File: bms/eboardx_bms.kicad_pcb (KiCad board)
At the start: 2 copper layers, 56 x 60 mm, 171 parts, among them J1 Balance connector, P1 CONN_1, P2 CONN_1, P3 CONN_1, P4 CONN_1, Q1 MMBT3904, Q10 SE4060GB, Q11 SE4060GB, Q12 SE4060GB, Q13 SE4060GB, Q14 MMBT3904, Q15 MMBT3906, Q16 MMBT3906, Q17 MMBT3906, Q18 MMBT3906, Q19 MMBT3906, Q2 SE4060GB, Q20 MMBT3906, Q21 MMBT3906, Q22 MMBT3906, Q23 MMBT3906, Q24 MMBT3906, Q25 MMBT3906, Q26 MMBT3906, Q27 A2SHB, Q28 A2SHB, Q29 A2SHB, Q3 SE4060GB, Q30 A2SHB, Q31 A2SHB, Q32 A2SHB, Q33 MMBT3906, Q34 MMBT3906, Q35 MMBT3906, Q36 MMBT3906, Q37 MMBT3906, Q38 MMBT3906, Q39 MMBT3906, Q4 SE4060GB, Q40 MMBT3906, Q41 A2SHB, Q42 A2SHB, Q43 A2SHB, Q44 A2SHB, Q5 SE4060GB, Q6 SE4060GB, Q7 SE4060GB, Q8 SE4060GB, Q9 SE4060GB, U1 DW01A, U10 HY2213-xxxA, U11 HY2213-xxxA, U12 HY2213-xxxA, U13 DW01A, U14 DW01A, U15 DW01A, U16 DW01A, U17 HY2213-xxxA, U18 HY2213-xxxA, U19 HY2213-xxxA, U2 DW01A, U20 HY2213-xxxA, U3 DW01A, U4 DW01A, U5 DW01A, U6 DW01A, U7 HY2213-xxxA, U8 HY2213-xxxA, U9 HY2213-xxxA

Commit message: bms
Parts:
- C14, C15, C16, C17, C2, C3, C4, C5, C6, C7, Q15, Q16, Q17, Q18, Q19, Q20, Q21, Q22, Q23, Q24, Q25, Q26, Q33, Q34, Q35, Q36, Q37, Q38, Q39, Q40, R10, R11, R12, R13, R14, R15, R16, R17, R18, R19, R20, R21, R22, R23, R24, R25, R26, R27, R28, R29, R30, R31, R32, R33, R34, R35, R36, R37, R38, R51, R52, R53, R54, R55, R56, R57, R58, R59, R60, R61, R62, R63, R64, R65, R66, R67, R69, R70, R71, R72, R9, U1, U13, U14, U15, U16, U2, U3, U4, U5, U6: moved to B.Cu
- P1: value CONN_1 -> BAT+
- P2: value CONN_1 -> P+
- P3: value CONN_1 -> P-
- P4: value CONN_1 -> BAT-
- moved R28 116.4 mm to (96.0, 93.1), turned to 90 degrees
- moved R25 116.3 mm to (98.1, 93.1), turned to 90 degrees
- moved R24 113.8 mm to (100.2, 93.1), turned to 90 degrees
- moved R21 113.7 mm to (102.3, 93.1), turned to 90 degrees
- moved R20 111.7 mm to (104.4, 93.1), turned to 90 degrees
- moved R17 111.6 mm to (106.5, 93.1), turned to 90 degrees
- moved R16 110.2 mm to (108.6, 93.1), turned to 90 degrees
- moved R13 110.1 mm to (110.7, 93.1), turned to 90 degrees
- moved R12 109.3 mm to (112.9, 93.1), turned to 90 degrees
- moved R9 109.3 mm to (115.0, 93.1), turned to 90 degrees
- moved Q24 109.1 mm to (97.1, 89.5), turned to 270 degrees
- moved Q22 106.3 mm to (101.3, 89.5), turned to 270 degrees
- moved Q20 104.0 mm to (105.5, 89.5), turned to 270 degrees
- moved Q18 102.4 mm to (109.7, 89.5), turned to 270 degrees
- moved Q23 102.3 mm to (97.1, 85.8), turned to 270 degrees
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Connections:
- C10 pad 2: Net-(C10-Pad2) -> /BAT4
- C11 pad 2: Net-(C11-Pad2) -> /BAT5
- C12 pad 2: Net-(C12-Pad2) -> /BAT6
- C13 pad 2: Net-(C13-Pad2) -> /BAT7
- C2 pad 2: Net-(C2-Pad2) -> /BAT2
- C3 pad 2: Net-(C3-Pad2) -> /BAT3
- C4 pad 2: Net-(C10-Pad2) -> /BAT4
- C5 pad 2: Net-(C11-Pad2) -> /BAT5
- C6 pad 2: Net-(C12-Pad2) -> /BAT6
- C7 pad 2: Net-(C13-Pad2) -> /BAT7
- C8 pad 2: Net-(C2-Pad2) -> /BAT2
- C9 pad 2: Net-(C3-Pad2) -> /BAT3
- J1 pad 1: /BAT- -> /BAT+
- J1 pad 10: /BAT2 -> /BAT10
- J1 pad 11: /BAT+ -> /BAT-
- J1 pad 2: /BAT10 -> /BAT2
- J1 pad 3: /BAT9 -> /BAT3
- J1 pad 4: /BAT8 -> /BAT4
- J1 pad 5: /BAT7 -> /BAT5
- J1 pad 7: /BAT5 -> /BAT7
- J1 pad 8: /BAT4 -> /BAT8
- J1 pad 9: /BAT3 -> /BAT9
- Q14 pad 2: /P -> /P-
- Q14 pad 3: Net-(Q10-Pad2) -> Net-(Q10-Pad1)
- Q17 pad 2: Net-(C2-Pad2) -> /BAT2
- Q18 pad 2: Net-(C2-Pad2) -> /BAT2
- Q19 pad 2: Net-(C3-Pad2) -> /BAT3
- Q2 pad 1: Net-(Q10-Pad1) -> Net-(Q1-Pad3)
- Q2 pad 2: Net-(Q1-Pad3) -> Net-(Q10-Pad2)
- Q20 pad 2: Net-(C3-Pad2) -> /BAT3
- Q21 pad 2: Net-(C10-Pad2) -> /BAT4
- Q22 pad 2: Net-(C10-Pad2) -> /BAT4
- Q23 pad 2: Net-(C11-Pad2) -> /BAT5
- Q24 pad 2: Net-(C11-Pad2) -> /BAT5
- Q25 pad 2: Net-(C12-Pad2) -> /BAT6
- Q26 pad 2: Net-(C12-Pad2) -> /BAT6
- Q27 pad 2: Net-(C2-Pad2) -> /BAT2
- Q28 pad 2: Net-(C3-Pad2) -> /BAT3
- Q29 pad 2: Net-(C10-Pad2) -> /BAT4
- Q3 pad 1: Net-(Q10-Pad1) -> Net-(Q1-Pad3)
- Q3 pad 2: Net-(Q1-Pad3) -> Net-(Q10-Pad2)
- Q30 pad 2: Net-(C11-Pad2) -> /BAT5
- Q31 pad 2: Net-(C12-Pad2) -> /BAT6
- Q32 pad 2: Net-(C13-Pad2) -> /BAT7
- Q4 pad 1: Net-(Q10-Pad1) -> Net-(Q1-Pad3)
- Q4 pad 2: Net-(Q1-Pad3) -> Net-(Q10-Pad2)
- Q5 pad 1: Net-(Q10-Pad1) -> Net-(Q1-Pad3)
- Q5 pad 2: Net-(Q1-Pad3) -> Net-(Q10-Pad2)
- Q6 pad 1: Net-(Q10-Pad1) -> Net-(Q1-Pad3)
- Q6 pad 2: Net-(Q1-Pad3) -> Net-(Q10-Pad2)
- Q7 pad 1: Net-(Q10-Pad1) -> Net-(Q1-Pad3)
- Q7 pad 2: Net-(Q1-Pad3) -> Net-(Q10-Pad2)
- R3 pad 1: Net-(Q10-Pad1) -> Net-(Q10-Pad2)
- R34 pad 1: Net-(C2-Pad2) -> /BAT2
- R35 pad 1: Net-(C3-Pad2) -> /BAT3
- R36 pad 1: Net-(C10-Pad2) -> /BAT4
- R37 pad 1: Net-(C11-Pad2) -> /BAT5
- R38 pad 1: Net-(C12-Pad2) -> /BAT6
- R40 pad 1: Net-(C2-Pad2) -> /BAT2
- R41 pad 1: Net-(C3-Pad2) -> /BAT3
- R42 pad 1: Net-(C10-Pad2) -> /BAT4
- R43 pad 1: Net-(C11-Pad2) -> /BAT5
- R44 pad 1: Net-(C12-Pad2) -> /BAT6
- R46 pad 1: Net-(C2-Pad2) -> /BAT2
- R47 pad 1: Net-(C3-Pad2) -> /BAT3
- R48 pad 1: Net-(C10-Pad2) -> /BAT4
- R49 pad 1: Net-(C11-Pad2) -> /BAT5
- R5 pad 1: Net-(Q10-Pad2) -> Net-(Q10-Pad1)
- R50 pad 1: Net-(C12-Pad2) -> /BAT6
- R6 pad 2: /P -> /P-
- R7 pad 1: /P -> /P-
- R7 pad 2: Net-(Q10-Pad2) -> Net-(Q10-Pad1)
- R8 pad 2: /P -> /P-
- U1 pad 2: Net-(C2-Pad2) -> /BAT2
- U1 pad 6: Net-(C2-Pad2) -> /BAT2
- U10 pad 3: Net-(C11-Pad2) -> /BAT5
- U11 pad 3: Net-(C12-Pad2) -> /BAT6
- U12 pad 3: Net-(C13-Pad2) -> /BAT7
- U2 pad 2: Net-(C3-Pad2) -> /BAT3
- U2 pad 6: Net-(C3-Pad2) -> /BAT3
- U3 pad 2: Net-(C10-Pad2) -> /BAT4
- U3 pad 6: Net-(C10-Pad2) -> /BAT4
- U4 pad 2: Net-(C11-Pad2) -> /BAT5
- U4 pad 6: Net-(C11-Pad2) -> /BAT5
- U5 pad 2: Net-(C12-Pad2) -> /BAT6
- U5 pad 6: Net-(C12-Pad2) -> /BAT6
- U6 pad 2: Net-(C13-Pad2) -> /BAT7
- U6 pad 6: Net-(C13-Pad2) -> /BAT7
- U7 pad 3: Net-(C2-Pad2) -> /BAT2
- U8 pad 3: Net-(C3-Pad2) -> /BAT3
- U9 pad 3: Net-(C10-Pad2) -> /BAT4
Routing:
- net /BAT4: track 0.00 -> 124.2 mm, vias 0 -> 2
- net /BAT3: track 0.00 -> 114.4 mm, vias 0 -> 2
- net /BAT5: track 0.00 -> 111.1 mm, vias 0 -> 2
- net /BAT6: track 0.00 -> 105.0 mm, vias 0 -> 3
- net /Balance charge and over current detection/OC5: track 0.00 -> 89.3 mm, vias 0 -> 4
- net /BAT2: track 0.00 -> 87.8 mm, vias 0 -> 2
- net /BAT8: track 0.00 -> 76.5 mm, vias 0 -> 2
- net /Balance charge and over current detection/OD5: track 0.00 -> 73.1 mm
- net Net-(Q1-Pad3): track 0.00 -> 69.2 mm
- net Net-(Q10-Pad1): track 0.00 -> 67.0 mm
- net /BAT7: track 0.00 -> 63.0 mm, vias 0 -> 2
- net /BAT10: track 0.00 -> 59.5 mm, vias 0 -> 1
- net /BAT9: track 0.00 -> 59.2 mm, vias 0 -> 2
- net /BAT+: track 0.00 -> 35.7 mm, vias 0 -> 3
- net /BAT-: track 0.00 -> 33.3 mm, vias 0 -> 18
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- added copper zone on B.Cu, net /BAT-
- added copper zone on F.Cu, net /BAT-
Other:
- net class Discharge added: clearance 0.2, trace_width 0.35, via_dia 0.8, via_drill 0.4
- net class Power added: clearance 0.2, trace_width 0.35, via_dia 1, via_drill 0.6
- net class Signal added: clearance 0.2, trace_width 0.2, via_dia 0.8, via_drill 0.4

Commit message: migrate to kicad7
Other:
- net class Default removed
- net class Discharge removed
- net class Power removed
- net class Signal removed

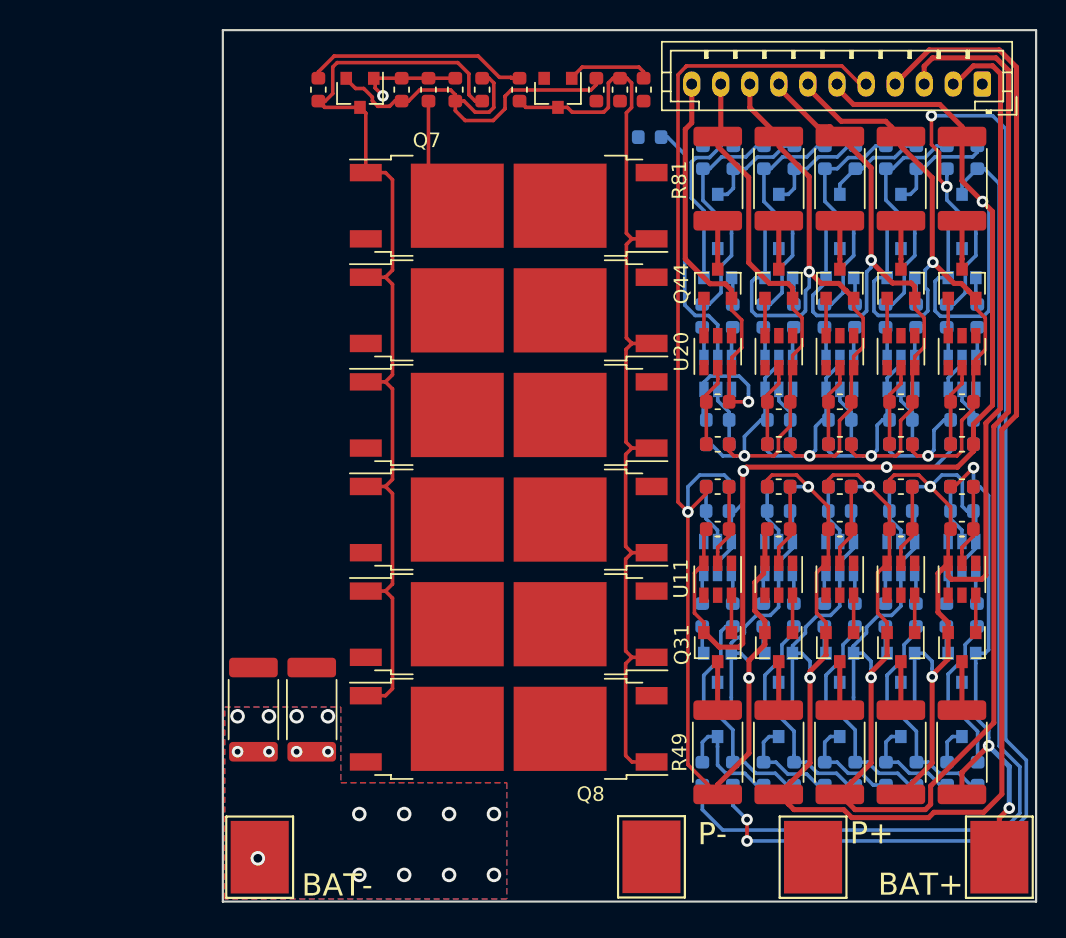
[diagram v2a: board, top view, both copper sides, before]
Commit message: update pcb footprints
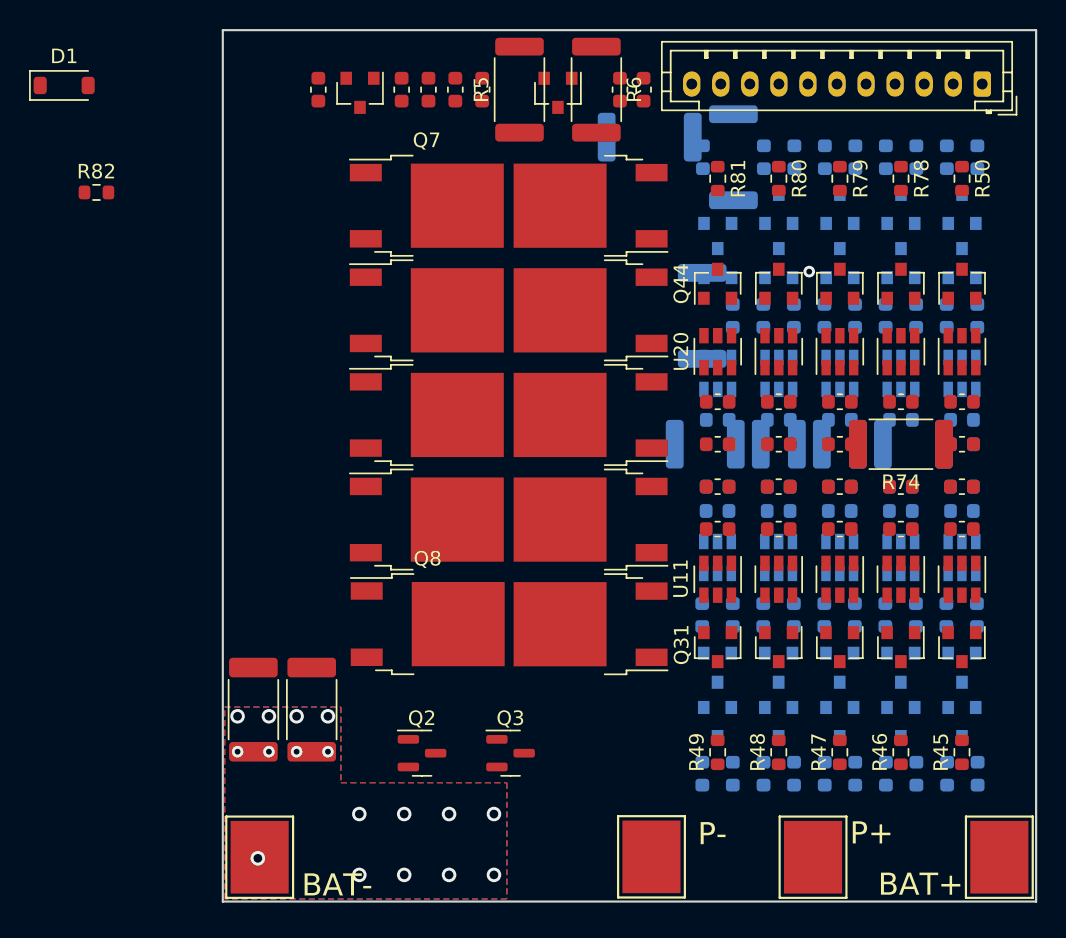
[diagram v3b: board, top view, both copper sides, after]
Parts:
- added D1: 1N4148W, Diode_SMD:D_SOD-123, F.Cu at (52.1, 45.7)
- added R82: 10M, Resistor_SMD:R_0603_1608Metric, F.Cu at (54.3, 53.1)
- C1: value 0.1u -> 470p
- Q1: value MMBT3904 -> BFS20
- Q10, Q11, Q12, Q13, Q4, Q5, Q6, Q7, Q8, Q9: value SE4060GB -> UMW 30N06
- Q14: value MMBT3904 -> MMBT5401
- Q15, Q16, Q17, Q18, Q19, Q20, Q21, Q22, Q23, Q24, Q25, Q26, Q33: value MMBT3906 -> MMBT5401
- Q2, Q3: value SE4060GB -> BFS20; footprint Package_TO_SOT_SMD:TO-252-2 -> Package_TO_SOT_SMD:SOT-23
- Q27, Q28, Q29, Q30, Q31, Q32: value A2SHB -> MMBT5401
- Q34, Q35, Q36, Q37, Q38, Q39, Q40: value MMBT3906 -> A2SHB
- R1: value 10M -> 1M
- R10, R11, R14, R56, R57, R60, R61, R64: value 510k -> 100
- R12, R13, R2, R3, R55, R58, R59, R62, R63, R8, R9: value 1M -> 100
- R15, R18, R19, R22, R23, R26, R27, R30, R31: value 510k -> 1M
- R33, R34, R75, R76, R77: value 100 -> 1M
- R35, R36, R37, R38, R39, R40, R41, R42, R43, R44: value 100 -> 510k
- R4: value 1M -> 1k
- R45, R46, R47, R48, R49, R50, R79: value 68 -> 510k; footprint Resistor_SMD:R_2512_6332Metric -> Resistor_SMD:R_0603_1608Metric
- R5: value 1M -> R005; footprint Resistor_SMD:R_0603_1608Metric -> Resistor_SMD:R_2512_6332Metric
- R51, R54: value 1M -> 510k
- R6: value 510k -> R005; footprint Resistor_SMD:R_0603_1608Metric -> Resistor_SMD:R_2512_6332Metric
- R65: value 510k -> 68; footprint Resistor_SMD:R_0603_1608Metric -> Resistor_SMD:R_2512_6332Metric
- R66: value 1M -> 68; footprint Resistor_SMD:R_0603_1608Metric -> Resistor_SMD:R_2512_6332Metric
- R67: value 1k -> 68; footprint Resistor_SMD:R_0603_1608Metric -> Resistor_SMD:R_2512_6332Metric
- R68, R73: value R004 -> 68
- R69, R70, R71, R72, R74: value 100 -> 68; footprint Resistor_SMD:R_0603_1608Metric -> Resistor_SMD:R_2512_6332Metric
- R7: value 10M -> 100
- R78, R81: value 68 -> 1M; footprint Resistor_SMD:R_2512_6332Metric -> Resistor_SMD:R_0603_1608Metric
- R80: value 68 -> 10M; footprint Resistor_SMD:R_2512_6332Metric -> Resistor_SMD:R_0603_1608Metric
- U1, U2, U3, U4, U5, U6: value DW01A -> DW01B
- U10, U7, U8, U9: value HY2213-xxxA -> DW01B
- U11, U12, U17, U18, U19, U20: value HY2213-xxxA -> HY2213-BB3A
- U13, U14, U15, U16: value DW01A -> HY2213-BB3A
- moved Q8 13.3 mm to (77.1, 82.8), turned to 0 degrees
- moved Q3 10.6 mm to (82.8, 91.7)
- moved Q2 1.71 mm to (76.7, 91.7)
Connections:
- C1 pad 1: /BO- -> Net-(Q1-E)
- C1 pad 2: /OD -> /DischargeControl
- C10 pad 1: Net-(C10-Pad1) -> Net-(U9-VCC)
- C10 pad 2: /BAT4 -> /BAT10
- C11 pad 1: Net-(C11-Pad1) -> Net-(U10-VCC)
- C11 pad 2: /BAT5 -> /BAT-
- C12 pad 1: Net-(C12-Pad1) -> Net-(U11-VCC)
- C12 pad 2: /BAT6 -> /BAT2
- C13 pad 1: Net-(C13-Pad1) -> Net-(U12-VCC)
- C13 pad 2: /BAT7 -> /BAT3
- C14 pad 1: Net-(C14-Pad1) -> Net-(U13-VCC)
- C14 pad 2: /BAT8 -> /BAT4
- C15 pad 1: Net-(C15-Pad1) -> Net-(U14-VCC)
- C15 pad 2: /BAT9 -> /BAT5
- C16 pad 1: Net-(C16-Pad1) -> Net-(U15-VCC)
- C16 pad 2: /BAT10 -> /BAT6
- C17 pad 1: Net-(C17-Pad1) -> Net-(U16-VCC)
- C17 pad 2: /BAT- -> /BAT7
- C18 pad 1: Net-(C18-Pad1) -> Net-(U17-VCC)
- C19 pad 1: Net-(C19-Pad1) -> Net-(U18-VCC)
- C2 pad 1: Net-(C2-Pad1) -> Net-(U1-VCC)
- C20 pad 1: Net-(C20-Pad1) -> Net-(U19-VCC)
- C21 pad 1: Net-(C21-Pad1) -> Net-(U20-VCC)
- C3 pad 1: Net-(C3-Pad1) -> Net-(U2-VCC)
- C4 pad 1: Net-(C4-Pad1) -> Net-(U3-VCC)
- C5 pad 1: Net-(C5-Pad1) -> Net-(U4-VCC)
- C6 pad 1: Net-(C6-Pad1) -> Net-(U5-VCC)
- C7 pad 1: Net-(C7-Pad1) -> Net-(U6-VCC)
- C8 pad 1: Net-(C8-Pad1) -> Net-(U7-VCC)
- C8 pad 2: /BAT2 -> /BAT8
- C9 pad 1: Net-(C9-Pad1) -> Net-(U8-VCC)
- C9 pad 2: /BAT3 -> /BAT9
- P3 pad 1: /P- -> /Pout-
- Q1 pad 1: /OD -> /DischargeControl
- Q1 pad 2: /BO- -> Net-(Q1-E)
- Q1 pad 3: Net-(Q1-Pad3) -> Net-(Q1-C)
- Q10 pad 1: Net-(Q10-Pad1) -> Net-(Q10-G)
- Q10 pad 2: Net-(Q10-Pad2) -> Net-(Q10-D)
- Q10 pad 3: /P- -> /Pout-
- Q11 pad 1: Net-(Q10-Pad1) -> Net-(Q10-G)
- Q11 pad 2: Net-(Q10-Pad2) -> Net-(Q10-D)
- Q11 pad 3: /P- -> /Pout-
- Q12 pad 1: Net-(Q10-Pad1) -> Net-(Q10-G)
- Q12 pad 2: Net-(Q10-Pad2) -> Net-(Q10-D)
- Q12 pad 3: /P- -> /Pout-
- Q13 pad 1: Net-(Q10-Pad1) -> Net-(Q10-G)
- Q13 pad 2: Net-(Q10-Pad2) -> Net-(Q10-D)
- Q13 pad 3: /P- -> /Pout-
- Q14 pad 1: /OC -> Net-(Q14-B)
- Q14 pad 2: /P- -> /BAT+
- Q14 pad 3: Net-(Q10-Pad1) -> Net-(Q14-C)
- Q15 pad 1: Net-(Q15-Pad1) -> Net-(Q15-B)
- Q15 pad 3: Net-(Q15-Pad3) -> Net-(Q15-C)
- Q16 pad 1: Net-(Q16-Pad1) -> Net-(Q16-B)
- Q16 pad 2: /BAT+ -> /BAT2
- Q16 pad 3: Net-(Q16-Pad3) -> /Balance charge and over current detection/OC1
- Q17 pad 1: Net-(Q17-Pad1) -> Net-(Q17-B)
- Q17 pad 3: /Balance charge and over current detection/OC1 -> /Balance charge and over current detection/OD1
- Q18 pad 1: Net-(Q18-Pad1) -> Net-(Q18-B)
- Q18 pad 2: /BAT2 -> /BAT3
- Q18 pad 3: /Balance charge and over current detection/OD1 -> /Balance charge and over current detection/OC2
- Q19 pad 1: Net-(Q19-Pad1) -> Net-(Q19-B)
- Q19 pad 3: /Balance charge and over current detection/OC2 -> /Balance charge and over current detection/OD2
- Q2 pad 1: Net-(Q1-Pad3) -> Net-(Q2-B)
- Q2 pad 2: Net-(Q10-Pad2) -> Net-(Q1-E)
- Q2 pad 3: /BO- -> Net-(Q1-C)
- Q20 pad 1: Net-(Q20-Pad1) -> Net-(Q20-B)
- Q20 pad 2: /BAT3 -> /BAT4
- Q20 pad 3: /Balance charge and over current detection/OD2 -> /Balance charge and over current detection/OC3
- Q21 pad 1: Net-(Q21-Pad1) -> Net-(Q21-B)
- Q21 pad 3: /Balance charge and over current detection/OC3 -> /Balance charge and over current detection/OD3
- Q22 pad 1: Net-(Q22-Pad1) -> Net-(Q22-B)
- Q22 pad 2: /BAT4 -> /BAT5
- Q22 pad 3: /Balance charge and over current detection/OD3 -> /Balance charge and over current detection/OC4
- Q23 pad 1: Net-(Q23-Pad1) -> Net-(Q23-B)
- Q23 pad 3: /Balance charge and over current detection/OC4 -> /Balance charge and over current detection/OD4
- Q24 pad 1: Net-(Q24-Pad1) -> Net-(Q24-B)
- Q24 pad 2: /BAT5 -> /BAT6
- Q24 pad 3: /Balance charge and over current detection/OD4 -> /Balance charge and over current detection/OC5
- Q25 pad 1: Net-(Q25-Pad1) -> Net-(Q25-B)
- Q25 pad 3: /Balance charge and over current detection/OC5 -> /Balance charge and over current detection/OD5
- Q26 pad 1: Net-(Q26-Pad1) -> Net-(Q26-B)
- Q26 pad 2: /BAT6 -> /BAT7
- Q26 pad 3: /Balance charge and over current detection/OD5 -> /Balance charge and over current detection/OC6
- Q27 pad 1: Net-(Q27-Pad1) -> Net-(Q27-B)
- Q27 pad 2: /BAT2 -> /BAT7
- Q27 pad 3: Net-(Q27-Pad3) -> /Balance charge and over current detection/OD6
- Q28 pad 1: Net-(Q28-Pad1) -> Net-(Q28-B)
- Q28 pad 2: /BAT3 -> /BAT8
- Q28 pad 3: Net-(Q28-Pad3) -> /Balance charge and over current detection/OC7
- Q29 pad 1: Net-(Q29-Pad1) -> Net-(Q29-B)
- Q29 pad 2: /BAT4 -> /BAT8
- Q29 pad 3: Net-(Q29-Pad3) -> /Balance charge and over current detection/OD7
- Q3 pad 1: Net-(Q1-Pad3) -> Net-(D1-K)
- Q3 pad 2: Net-(Q10-Pad2) -> /P-
- Q3 pad 3: /BO- -> Net-(Q10-G)
- Q30 pad 1: Net-(Q30-Pad1) -> Net-(Q30-B)
- Q30 pad 2: /BAT5 -> /BAT9
- Q30 pad 3: Net-(Q30-Pad3) -> /Balance charge and over current detection/OC8
- Q31 pad 1: Net-(Q31-Pad1) -> Net-(Q31-B)
- Q31 pad 2: /BAT6 -> /BAT9
- Q31 pad 3: Net-(Q31-Pad3) -> /Balance charge and over current detection/OD8
- Q32 pad 1: Net-(Q32-Pad1) -> Net-(Q32-B)
- Q32 pad 2: /BAT7 -> /BAT10
- Q32 pad 3: Net-(Q32-Pad3) -> /Balance charge and over current detection/OC9
- Q33 pad 1: Net-(Q33-Pad1) -> Net-(Q33-B)
- Q33 pad 2: /BAT7 -> /BAT10
- Q33 pad 3: /Balance charge and over current detection/OC6 -> /Balance charge and over current detection/OD9
- Q34 pad 1: Net-(Q34-Pad1) -> Net-(Q34-G)
- Q34 pad 2: /BAT7 -> /BAT2
- Q34 pad 3: /Balance charge and over current detection/OD6 -> Net-(Q34-D)
- Q35 pad 1: Net-(Q35-Pad1) -> Net-(Q35-G)
- Q35 pad 2: /BAT8 -> /BAT3
- Q35 pad 3: /Balance charge and over current detection/OC7 -> Net-(Q35-D)
- Q36 pad 1: Net-(Q36-Pad1) -> Net-(Q36-G)
- Q36 pad 2: /BAT8 -> /BAT4
- Q36 pad 3: /Balance charge and over current detection/OD7 -> Net-(Q36-D)
- Q37 pad 1: Net-(Q37-Pad1) -> Net-(Q37-G)
- Q37 pad 2: /BAT9 -> /BAT5
- Q37 pad 3: /Balance charge and over current detection/OC8 -> Net-(Q37-D)
- Q38 pad 1: Net-(Q38-Pad1) -> Net-(Q38-G)
- Q38 pad 2: /BAT9 -> /BAT6
- Q38 pad 3: /Balance charge and over current detection/OD8 -> Net-(Q38-D)
- Q39 pad 1: Net-(Q39-Pad1) -> Net-(Q39-G)
- Q39 pad 2: /BAT10 -> /BAT7
- Q39 pad 3: /Balance charge and over current detection/OC9 -> Net-(Q39-D)
- Q4 pad 1: Net-(Q1-Pad3) -> Net-(Q1-C)
- Q4 pad 2: Net-(Q10-Pad2) -> Net-(Q10-D)
- Q4 pad 3: /BO- -> /BatOut-
- Q40 pad 1: Net-(Q40-Pad1) -> Net-(Q40-G)
- Q40 pad 2: /BAT10 -> /BAT8
- Q40 pad 3: /Balance charge and over current detection/OD9 -> Net-(Q40-D)
- Q41 pad 1: Net-(Q41-Pad1) -> Net-(Q41-G)
- Q41 pad 2: /BAT8 -> /BAT9
- Q41 pad 3: Net-(Q41-Pad3) -> Net-(Q41-D)
- Q42 pad 1: Net-(Q42-Pad1) -> Net-(Q42-G)
- Q42 pad 2: /BAT9 -> /BAT10
- Q42 pad 3: Net-(Q42-Pad3) -> Net-(Q42-D)
- Q43 pad 1: Net-(Q43-Pad1) -> Net-(Q43-G)
- Q43 pad 2: /BAT10 -> /BAT-
- Q43 pad 3: Net-(Q43-Pad3) -> Net-(Q43-D)
- Q5 pad 1: Net-(Q1-Pad3) -> Net-(Q1-C)
- Q5 pad 2: Net-(Q10-Pad2) -> Net-(Q10-D)
- Q5 pad 3: /BO- -> /BatOut-
- Q6 pad 1: Net-(Q1-Pad3) -> Net-(Q1-C)
- Q6 pad 2: Net-(Q10-Pad2) -> Net-(Q10-D)
- Q6 pad 3: /BO- -> /BatOut-
- Q7 pad 1: Net-(Q1-Pad3) -> Net-(Q1-C)
- Q7 pad 2: Net-(Q10-Pad2) -> Net-(Q10-D)
- Q7 pad 3: /BO- -> /BatOut-
- Q8 pad 1: Net-(Q10-Pad1) -> Net-(Q1-C)
- Q8 pad 2: Net-(Q10-Pad2) -> Net-(Q10-D)
- Q8 pad 3: /P- -> /BatOut-
- Q9 pad 1: Net-(Q10-Pad1) -> Net-(Q10-G)
- Q9 pad 2: Net-(Q10-Pad2) -> Net-(Q10-D)
- Q9 pad 3: /P- -> /Pout-
- R1 pad 1: /BO- -> Net-(Q2-B)
- R1 pad 2: Net-(Q1-Pad3) -> Net-(Q1-E)
- R10 pad 1: Net-(Q15-Pad1) -> /BAT6
- R10 pad 2: Net-(R10-Pad2) -> Net-(U6-VCC)
- R11 pad 1: Net-(Q16-Pad1) -> /BAT7
- R11 pad 2: Net-(R11-Pad2) -> Net-(U7-VCC)
- R12 pad 1: /Balance charge and over current detection/OD1 -> /BAT8
- R12 pad 2: Net-(Q16-Pad3) -> Net-(U8-VCC)
- R13 pad 1: /Balance charge and over current detection/OC2 -> /BAT9
- R13 pad 2: /Balance charge and over current detection/OC1 -> Net-(U9-VCC)
- R14 pad 1: Net-(Q17-Pad1) -> /BAT10
- R14 pad 2: Net-(R14-Pad2) -> Net-(U10-VCC)
- R15 pad 1: Net-(Q18-Pad1) -> /Balance charge and over current detection/OC1
- R15 pad 2: Net-(R15-Pad2) -> Net-(Q14-C)
- R16 pad 1: /Balance charge and over current detection/OD2 -> /Balance charge and over current detection/OD1
- R16 pad 2: /Balance charge and over current detection/OD1 -> Net-(Q15-C)
- R17 pad 1: /Balance charge and over current detection/OC3 -> /Balance charge and over current detection/OC2
- R17 pad 2: /Balance charge and over current detection/OC2 -> /Balance charge and over current detection/OC1
- R18 pad 1: Net-(Q19-Pad1) -> /Balance charge and over current detection/OD2
- R18 pad 2: Net-(R18-Pad2) -> /Balance charge and over current detection/OD1
- R19 pad 1: Net-(Q20-Pad1) -> /Balance charge and over current detection/OC3
- R19 pad 2: Net-(R19-Pad2) -> /Balance charge and over current detection/OC2
- R2 pad 1: /OD -> /BAT+
- R2 pad 2: /BO- -> Net-(U1-VCC)
- R22 pad 1: Net-(Q21-Pad1) -> /Balance charge and over current detection/OD4
- R22 pad 2: Net-(R22-Pad2) -> /Balance charge and over current detection/OD3
- R23 pad 1: Net-(Q22-Pad1) -> /Balance charge and over current detection/OC5
- R23 pad 2: Net-(R23-Pad2) -> /Balance charge and over current detection/OC4
- R24 pad 1: /Balance charge and over current detection/OD4 -> /Balance charge and over current detection/OD5
- R24 pad 2: /Balance charge and over current detection/OD3 -> /Balance charge and over current detection/OD4
- R25 pad 1: /Balance charge and over current detection/OC5 -> /Balance charge and over current detection/OC6
- R25 pad 2: /Balance charge and over current detection/OC4 -> /Balance charge and over current detection/OC5
- R26 pad 1: Net-(Q23-Pad1) -> /Balance charge and over current detection/OD6
- R26 pad 2: Net-(R26-Pad2) -> /Balance charge and over current detection/OD5
- R27 pad 1: Net-(Q24-Pad1) -> /Balance charge and over current detection/OC7
- R27 pad 2: Net-(R27-Pad2) -> /Balance charge and over current detection/OC6
- R28 pad 1: /Balance charge and over current detection/OD5 -> /Balance charge and over current detection/OD7
- R28 pad 2: /Balance charge and over current detection/OD4 -> /Balance charge and over current detection/OD6
- R29 pad 1: /Balance charge and over current detection/OC6 -> /Balance charge and over current detection/OC8
- R29 pad 2: /Balance charge and over current detection/OC5 -> /Balance charge and over current detection/OC7
- R3 pad 1: Net-(Q10-Pad2) -> /BAT2
- R3 pad 2: /OD -> Net-(U2-VCC)
- R30 pad 1: Net-(Q25-Pad1) -> /Balance charge and over current detection/OD8
- R30 pad 2: Net-(R30-Pad2) -> /Balance charge and over current detection/OD7
- R31 pad 1: Net-(Q26-Pad1) -> /Balance charge and over current detection/OC9
- R31 pad 2: Net-(R31-Pad2) -> /Balance charge and over current detection/OC8
- R32 pad 1: /Balance charge and over current detection/OD6 -> /Balance charge and over current detection/OD9
- R32 pad 2: /Balance charge and over current detection/OD5 -> /Balance charge and over current detection/OD8
- R33 pad 1: /BAT+ -> /ChargeControl
- R33 pad 2: Net-(C2-Pad1) -> /Balance charge and over current detection/OC9
- R34 pad 1: /BAT2 -> /DischargeControl
- R34 pad 2: Net-(C3-Pad1) -> /Balance charge and over current detection/OD9
- R35 pad 1: /BAT3 -> Net-(Q14-B)
- R35 pad 2: Net-(C4-Pad1) -> Net-(U1-OC)
- R36 pad 1: /BAT4 -> Net-(Q15-B)
- R36 pad 2: Net-(C5-Pad1) -> Net-(U1-OD)
- R37 pad 1: /BAT5 -> Net-(Q16-B)
- R37 pad 2: Net-(C6-Pad1) -> Net-(U2-OC)
- R38 pad 1: /BAT6 -> Net-(Q17-B)
- R38 pad 2: Net-(C7-Pad1) -> Net-(U2-OD)
- R39 pad 1: /BAT+ -> Net-(Q18-B)
- R39 pad 2: Net-(C8-Pad1) -> Net-(U3-OC)
- R4 pad 1: Net-(Q1-Pad3) -> Net-(U10-CS)
- R4 pad 2: /BAT8 -> /BatOut-
- R40 pad 1: /BAT2 -> Net-(Q19-B)
- R40 pad 2: Net-(C9-Pad1) -> Net-(U3-OD)
- R41 pad 1: /BAT3 -> Net-(Q20-B)
- R41 pad 2: Net-(C10-Pad1) -> Net-(U4-OC)
- R42 pad 1: /BAT4 -> Net-(Q21-B)
- R42 pad 2: Net-(C11-Pad1) -> Net-(U4-OD)
- R43 pad 1: /BAT5 -> Net-(Q22-B)
- R43 pad 2: Net-(C12-Pad1) -> Net-(U5-OC)
- R44 pad 1: /BAT6 -> Net-(Q23-B)
- R44 pad 2: Net-(C13-Pad1) -> Net-(U5-OD)
- R45 pad 1: /BAT+ -> Net-(Q24-B)
- R45 pad 2: Net-(Q27-Pad3) -> Net-(U6-OC)
- R46 pad 1: /BAT2 -> Net-(Q25-B)
- R46 pad 2: Net-(Q28-Pad3) -> Net-(U6-OD)
- R47 pad 1: /BAT3 -> Net-(Q26-B)
- R47 pad 2: Net-(Q29-Pad3) -> Net-(U7-OC)
- R48 pad 1: /BAT4 -> Net-(Q27-B)
- R48 pad 2: Net-(Q30-Pad3) -> Net-(U7-OD)
- R49 pad 1: /BAT5 -> Net-(Q28-B)
- R49 pad 2: Net-(Q31-Pad3) -> Net-(U8-OC)
- R5 pad 1: Net-(Q10-Pad1) -> /BAT-
- R5 pad 2: /BAT8 -> /BatOut-
- R50 pad 1: /BAT6 -> Net-(Q29-B)
- R50 pad 2: Net-(Q32-Pad3) -> Net-(U8-OD)
- R51 pad 1: /Balance charge and over current detection/OC7 -> Net-(Q30-B)
- R51 pad 2: /Balance charge and over current detection/OC6 -> Net-(U9-OC)
- R52 pad 1: Net-(Q33-Pad1) -> Net-(Q31-B)
- R52 pad 2: Net-(R52-Pad2) -> Net-(U9-OD)
- R53 pad 1: Net-(Q34-Pad1) -> Net-(Q32-B)
- R53 pad 2: Net-(R53-Pad2) -> Net-(U10-OC)
- R54 pad 1: /Balance charge and over current detection/OD7 -> Net-(Q33-B)
- R54 pad 2: /Balance charge and over current detection/OD6 -> Net-(U10-OD)
- R55 pad 1: /Balance charge and over current detection/OC8 -> /BAT+
- R55 pad 2: /Balance charge and over current detection/OC7 -> Net-(U11-VCC)
- R56 pad 1: Net-(Q35-Pad1) -> /BAT2
- R56 pad 2: Net-(R56-Pad2) -> Net-(U12-VCC)
- R57 pad 1: Net-(Q36-Pad1) -> /BAT3
- R57 pad 2: Net-(R57-Pad2) -> Net-(U13-VCC)
- R58 pad 1: /Balance charge and over current detection/OD8 -> /BAT4
- R58 pad 2: /Balance charge and over current detection/OD7 -> Net-(U14-VCC)
- R59 pad 1: /Balance charge and over current detection/OC9 -> /BAT5
- R59 pad 2: /Balance charge and over current detection/OC8 -> Net-(U15-VCC)
- R6 pad 1: /BO- -> /BAT-
- R6 pad 2: /P- -> /BatOut-
- R60 pad 1: Net-(Q37-Pad1) -> /BAT6
- R60 pad 2: Net-(R60-Pad2) -> Net-(U16-VCC)
- R61 pad 1: Net-(Q38-Pad1) -> /BAT7
- R61 pad 2: Net-(R61-Pad2) -> Net-(U17-VCC)
- R62 pad 1: /Balance charge and over current detection/OD9 -> /BAT8
- R62 pad 2: /Balance charge and over current detection/OD8 -> Net-(U18-VCC)
- R63 pad 1: /OC -> /BAT9
- R63 pad 2: /Balance charge and over current detection/OC9 -> Net-(U19-VCC)
- R64 pad 1: Net-(Q39-Pad1) -> /BAT10
- R64 pad 2: Net-(R64-Pad2) -> Net-(U20-VCC)
- R65 pad 1: Net-(Q40-Pad1) -> /BAT+
- R65 pad 2: Net-(R65-Pad2) -> Net-(Q34-D)
- R66 pad 1: /OD -> /BAT2
- R66 pad 2: /Balance charge and over current detection/OD9 -> Net-(Q35-D)
- R67 pad 1: Net-(R67-Pad1) -> /BAT3
- R67 pad 2: /BO- -> Net-(Q36-D)
- R68 pad 1: /BAT- -> /BAT4
- R68 pad 2: /BO- -> Net-(Q37-D)
- R69 pad 1: /BAT7 -> /BAT5
- R69 pad 2: Net-(C14-Pad1) -> Net-(Q38-D)
- R7 pad 1: /P- -> /BAT3
- R7 pad 2: Net-(Q10-Pad1) -> Net-(U3-VCC)
- R70 pad 1: /BAT8 -> /BAT6
- R70 pad 2: Net-(C15-Pad1) -> Net-(Q39-D)
- R71 pad 1: /BAT9 -> /BAT7
- R71 pad 2: Net-(C16-Pad1) -> Net-(Q40-D)
- R72 pad 1: /BAT10 -> /BAT8
- R72 pad 2: Net-(C17-Pad1) -> Net-(Q41-D)
- R73 pad 1: /BAT- -> /BAT9
- R73 pad 2: /BO- -> Net-(Q42-D)
- R74 pad 1: /BAT7 -> /BAT10
- R74 pad 2: Net-(C18-Pad1) -> Net-(Q43-D)
- R75 pad 1: /BAT8 -> Net-(Q1-E)
- R75 pad 2: Net-(C19-Pad1) -> /DischargeControl
- R76 pad 1: /BAT9 -> Net-(Q10-D)
- R76 pad 2: Net-(C20-Pad1) -> Net-(Q2-B)
- R77 pad 1: /BAT10 -> Net-(Q1-C)
- R77 pad 2: Net-(C21-Pad1) -> /BAT7
- R78 pad 1: /BAT7 -> Net-(Q10-G)
- R78 pad 2: Net-(Q41-Pad3) -> /BAT7
- R79 pad 1: /BAT8 -> /BAT-
- R79 pad 2: Net-(Q42-Pad3) -> /P-
- R8 pad 1: /OC -> /BAT4
- R8 pad 2: /P- -> Net-(U4-VCC)
- R80 pad 1: /BAT9 -> /P-
- R80 pad 2: Net-(Q43-Pad3) -> Net-(Q10-G)
- R81 pad 1: /BAT10 -> Net-(D1-K)
- R81 pad 2: Net-(Q44-Pad3) -> /P-
- R9 pad 1: /Balance charge and over current detection/OC1 -> /BAT5
- R9 pad 2: Net-(Q15-Pad3) -> Net-(U5-VCC)
- U1 pad 1: Net-(R11-Pad2) -> Net-(U1-OD)
- U1 pad 3: Net-(R10-Pad2) -> Net-(U1-OC)
- U1 pad 4: Net-(U1-Pad4) -> unconnected-(U1-TD-Pad4)
- U1 pad 5: Net-(C2-Pad1) -> Net-(U1-VCC)
- U10 pad 1: Net-(U10-Pad1) -> Net-(U10-OD)
- U10 pad 2: Net-(C11-Pad1) -> Net-(U10-CS)
- U10 pad 3: /BAT5 -> Net-(U10-OC)
- U10 pad 4: Net-(U10-Pad4) -> unconnected-(U10-TD-Pad4)
- U10 pad 5: Net-(U10-Pad5) -> Net-(U10-VCC)
- U10 pad 6: Net-(Q30-Pad1) -> /BAT-
- U11 pad 1: Net-(U11-Pad1) -> unconnected-(U11-NC-Pad1)
- U11 pad 2: Net-(C12-Pad1) -> Net-(U11-VCC)
- U11 pad 3: /BAT6 -> /BAT2
- U11 pad 4: Net-(U11-Pad4) -> unconnected-(U11-NC-Pad4)
- U11 pad 5: Net-(U11-Pad5) -> unconnected-(U11-NC-Pad5)
- U11 pad 6: Net-(Q31-Pad1) -> Net-(Q34-G)
- U12 pad 1: Net-(U12-Pad1) -> unconnected-(U12-NC-Pad1)
- U12 pad 2: Net-(C13-Pad1) -> Net-(U12-VCC)
- U12 pad 3: /BAT7 -> /BAT3
- U12 pad 4: Net-(U12-Pad4) -> unconnected-(U12-NC-Pad4)
- U12 pad 5: Net-(U12-Pad5) -> unconnected-(U12-NC-Pad5)
- U12 pad 6: Net-(Q32-Pad1) -> Net-(Q35-G)
- U13 pad 1: Net-(R53-Pad2) -> unconnected-(U13-NC-Pad1)
- U13 pad 2: /BAT8 -> Net-(U13-VCC)
- U13 pad 3: Net-(R52-Pad2) -> /BAT4
- U13 pad 4: Net-(U13-Pad4) -> unconnected-(U13-NC-Pad4)
- U13 pad 5: Net-(C14-Pad1) -> unconnected-(U13-NC-Pad5)
- U13 pad 6: /BAT8 -> Net-(Q36-G)
- U14 pad 1: Net-(R57-Pad2) -> unconnected-(U14-NC-Pad1)
- U14 pad 2: /BAT9 -> Net-(U14-VCC)
- U14 pad 3: Net-(R56-Pad2) -> /BAT5
- U14 pad 4: Net-(U14-Pad4) -> unconnected-(U14-NC-Pad4)
- U14 pad 5: Net-(C15-Pad1) -> unconnected-(U14-NC-Pad5)
- U14 pad 6: /BAT9 -> Net-(Q37-G)
- U15 pad 1: Net-(R61-Pad2) -> unconnected-(U15-NC-Pad1)
- U15 pad 2: /BAT10 -> Net-(U15-VCC)
- U15 pad 3: Net-(R60-Pad2) -> /BAT6
- U15 pad 4: Net-(U15-Pad4) -> unconnected-(U15-NC-Pad4)
- U15 pad 5: Net-(C16-Pad1) -> unconnected-(U15-NC-Pad5)
- U15 pad 6: /BAT10 -> Net-(Q38-G)
- U16 pad 1: Net-(R65-Pad2) -> unconnected-(U16-NC-Pad1)
- U16 pad 2: Net-(R67-Pad1) -> Net-(U16-VCC)
- U16 pad 3: Net-(R64-Pad2) -> /BAT7
- U16 pad 4: Net-(U16-Pad4) -> unconnected-(U16-NC-Pad4)
- U16 pad 5: Net-(C17-Pad1) -> unconnected-(U16-NC-Pad5)
- U16 pad 6: /BAT- -> Net-(Q39-G)
- U17 pad 1: Net-(U17-Pad1) -> unconnected-(U17-NC-Pad1)
- U17 pad 2: Net-(C18-Pad1) -> Net-(U17-VCC)
- U17 pad 4: Net-(U17-Pad4) -> unconnected-(U17-NC-Pad4)
- U17 pad 5: Net-(U17-Pad5) -> unconnected-(U17-NC-Pad5)
- U17 pad 6: Net-(Q41-Pad1) -> Net-(Q40-G)
- U18 pad 1: Net-(U18-Pad1) -> unconnected-(U18-NC-Pad1)
- U18 pad 2: Net-(C19-Pad1) -> Net-(U18-VCC)
- U18 pad 4: Net-(U18-Pad4) -> unconnected-(U18-NC-Pad4)
- U18 pad 5: Net-(U18-Pad5) -> unconnected-(U18-NC-Pad5)
- U18 pad 6: Net-(Q42-Pad1) -> Net-(Q41-G)
- U19 pad 1: Net-(U19-Pad1) -> unconnected-(U19-NC-Pad1)
- U19 pad 2: Net-(C20-Pad1) -> Net-(U19-VCC)
- U19 pad 4: Net-(U19-Pad4) -> unconnected-(U19-NC-Pad4)
- U19 pad 5: Net-(U19-Pad5) -> unconnected-(U19-NC-Pad5)
- U19 pad 6: Net-(Q43-Pad1) -> Net-(Q42-G)
- U2 pad 1: Net-(R15-Pad2) -> Net-(U2-OD)
- U2 pad 3: Net-(R14-Pad2) -> Net-(U2-OC)
- U2 pad 4: Net-(U2-Pad4) -> unconnected-(U2-TD-Pad4)
- U2 pad 5: Net-(C3-Pad1) -> Net-(U2-VCC)
- U20 pad 1: Net-(U20-Pad1) -> unconnected-(U20-NC-Pad1)
- U20 pad 2: Net-(C21-Pad1) -> Net-(U20-VCC)
- U20 pad 4: Net-(U20-Pad4) -> unconnected-(U20-NC-Pad4)
- U20 pad 5: Net-(U20-Pad5) -> unconnected-(U20-NC-Pad5)
- U20 pad 6: Net-(Q44-Pad1) -> Net-(Q43-G)
- U3 pad 1: Net-(R19-Pad2) -> Net-(U3-OD)
- U3 pad 3: Net-(R18-Pad2) -> Net-(U3-OC)
- U3 pad 4: Net-(U3-Pad4) -> unconnected-(U3-TD-Pad4)
- U3 pad 5: Net-(C4-Pad1) -> Net-(U3-VCC)
- U4 pad 1: Net-(R23-Pad2) -> Net-(U4-OD)
- U4 pad 3: Net-(R22-Pad2) -> Net-(U4-OC)
- U4 pad 4: Net-(U4-Pad4) -> unconnected-(U4-TD-Pad4)
- U4 pad 5: Net-(C5-Pad1) -> Net-(U4-VCC)
- U5 pad 1: Net-(R27-Pad2) -> Net-(U5-OD)
- U5 pad 3: Net-(R26-Pad2) -> Net-(U5-OC)
- U5 pad 4: Net-(U5-Pad4) -> unconnected-(U5-TD-Pad4)
- U5 pad 5: Net-(C6-Pad1) -> Net-(U5-VCC)
- U6 pad 1: Net-(R31-Pad2) -> Net-(U6-OD)
- U6 pad 3: Net-(R30-Pad2) -> Net-(U6-OC)
- U6 pad 4: Net-(U6-Pad4) -> unconnected-(U6-TD-Pad4)
- U6 pad 5: Net-(C7-Pad1) -> Net-(U6-VCC)
- U7 pad 1: Net-(U7-Pad1) -> Net-(U7-OD)
- U7 pad 2: Net-(C8-Pad1) -> /BAT8
- U7 pad 3: /BAT2 -> Net-(U7-OC)
- U7 pad 4: Net-(U7-Pad4) -> unconnected-(U7-TD-Pad4)
- U7 pad 5: Net-(U7-Pad5) -> Net-(U7-VCC)
- U7 pad 6: Net-(Q27-Pad1) -> /BAT8
- U8 pad 1: Net-(U8-Pad1) -> Net-(U8-OD)
- U8 pad 2: Net-(C9-Pad1) -> /BAT9
- U8 pad 3: /BAT3 -> Net-(U8-OC)
- U8 pad 4: Net-(U8-Pad4) -> unconnected-(U8-TD-Pad4)
- U8 pad 5: Net-(U8-Pad5) -> Net-(U8-VCC)
- U8 pad 6: Net-(Q28-Pad1) -> /BAT9
- U9 pad 1: Net-(U9-Pad1) -> Net-(U9-OD)
- U9 pad 2: Net-(C10-Pad1) -> /BAT10
- U9 pad 3: /BAT4 -> Net-(U9-OC)
- U9 pad 4: Net-(U9-Pad4) -> unconnected-(U9-TD-Pad4)
- U9 pad 5: Net-(U9-Pad5) -> Net-(U9-VCC)
- U9 pad 6: Net-(Q29-Pad1) -> /BAT10
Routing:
- net /BAT4: track 124.2 -> 0.00 mm
- net /BAT3: track 114.4 -> 0.00 mm, vias 2 -> 0
- net /BAT5: track 111.1 -> 0.00 mm, vias 2 -> 0
- net /BAT6: track 105.0 -> 0.00 mm, vias 3 -> 0
- net /Balance charge and over current detection/OC5: track 89.3 -> 0.00 mm, vias 4 -> 0
- net /BAT2: track 87.8 -> 0.00 mm, vias 2 -> 0
- net /BAT8: track 76.5 -> 0.00 mm, vias 2 -> 0
- net /Balance charge and over current detection/OD5: track 73.1 -> 0.00 mm
- net Net-(Q1-Pad3): track 69.2 -> 0.00 mm
- net Net-(Q10-Pad1): track 67.0 -> 0.00 mm
- net /BAT7: track 63.0 -> 0.00 mm, vias 2 -> 0
- net /BAT10: track 59.5 -> 0.00 mm, vias 1 -> 0
- net /BAT9: track 59.2 -> 0.00 mm, vias 2 -> 3
- net /BAT+: track 35.7 -> 0.00 mm, vias 3 -> 0
- net /BAT-: track 33.3 -> 0.00 mm, vias 18 -> 13
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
